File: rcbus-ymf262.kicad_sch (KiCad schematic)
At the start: 41 parts, among them CON1 SJ1-3523N, P1 RC2014 BUS, U1 74HCT688, U2 YMF262, U3 YAC512, U4 TL074, Y1 SG-8002CA

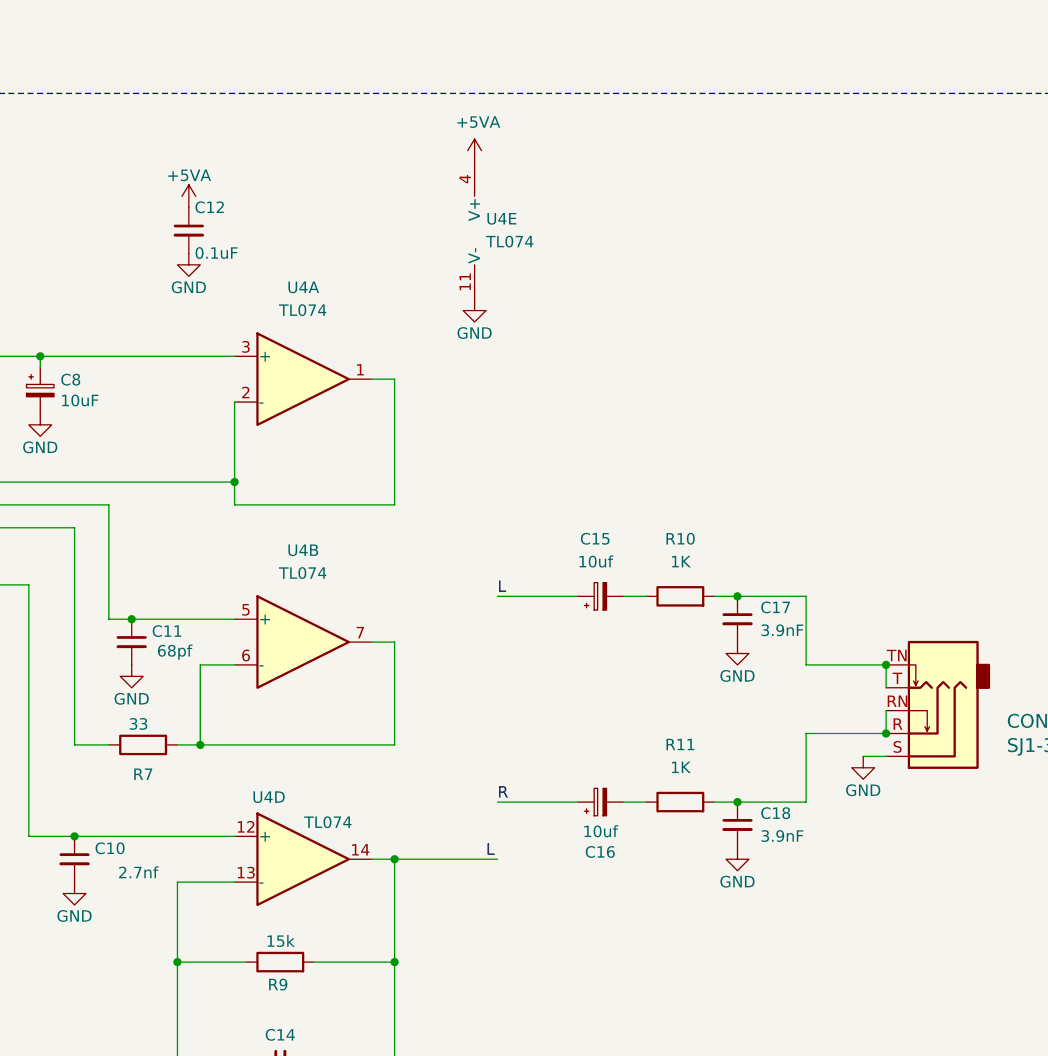
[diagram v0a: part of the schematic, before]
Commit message: remove some components, more tidyup
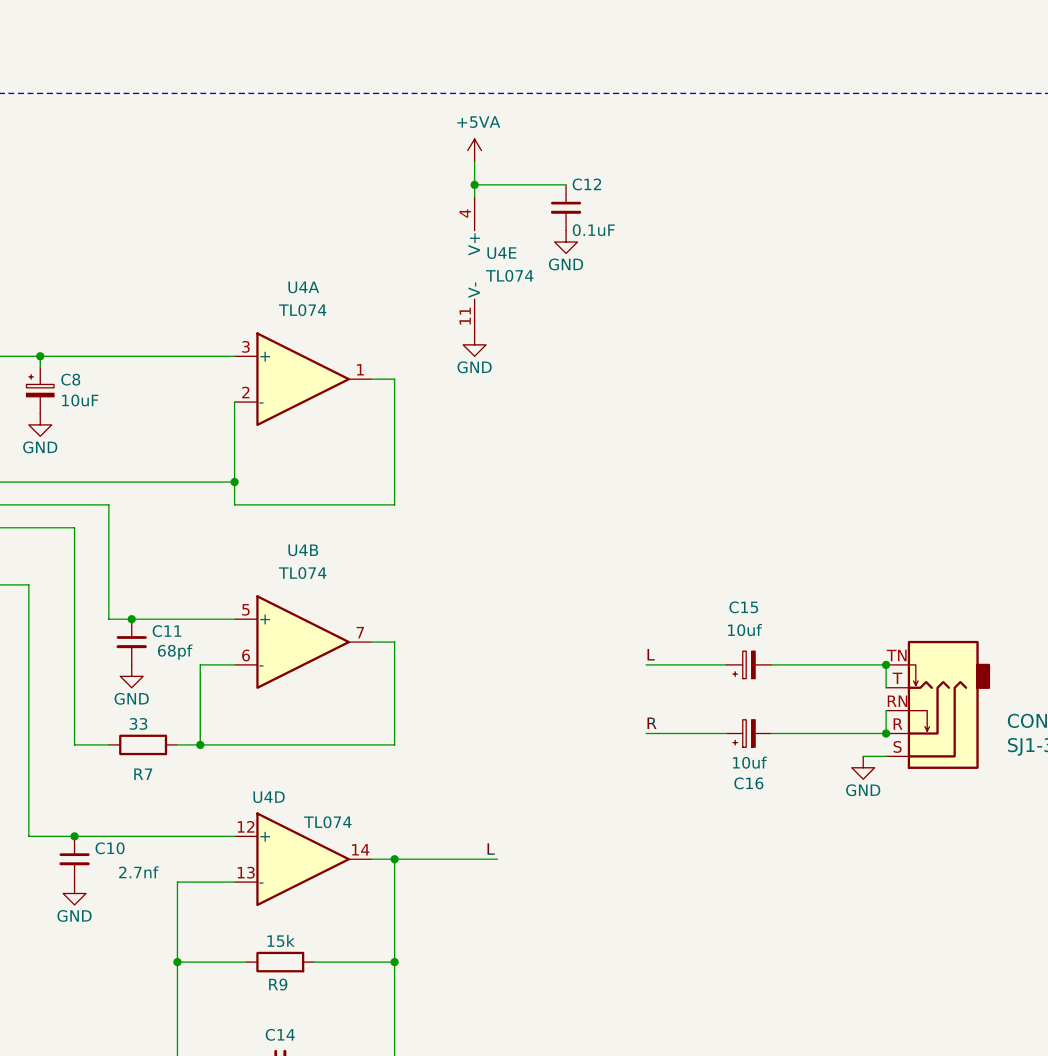
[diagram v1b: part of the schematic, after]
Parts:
- removed C17, C18: 3.9nF, Capacitor_SMD:C_0603_1608Metric_Pad1.08x0.95mm_HandSolder, symbol Device:C_Small
- removed R10, R11: 1K, Resistor_SMD:R_0603_1608Metric_Pad0.98x0.95mm_HandSolder, symbol Device:R
- C1, C10, C11, C12, C13, C14, C19, C2, C3, C6, C7, C8, C9: footprint Capacitor_SMD:C_0603_1608Metric_Pad1.08x0.95mm_HandSolder -> Capacitor_SMD:C_0603_1608Metric
- C15, C16: footprint Capacitor_SMD:C_0603_1608Metric_Pad1.08x0.95mm_HandSolder -> Capacitor_SMD:C_1206_3216Metric
- L1, L2: footprint Inductor_SMD:L_0603_1608Metric_Pad1.05x0.95mm_HandSolder -> Inductor_SMD:L_0603_1608Metric
- R1, R2, R3, R4, R5, R6, R7, R8, R9: footprint Resistor_SMD:R_0603_1608Metric_Pad0.98x0.95mm_HandSolder -> Resistor_SMD:R_0603_1608Metric
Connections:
- net at CON1.R, CON1.RN: now also C16.2
- net at CON1.T, CON1.TN: now also C15.2
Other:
- moved on the sheet: C12, C15, C16, U4E
